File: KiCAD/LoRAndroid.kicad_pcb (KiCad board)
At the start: 4 copper layers, 35 x 14 mm, 55 parts, among them J1 SMA, P1 DX07P022AA6R2000, U1 MIC5504-3.3YMT, U2 SX1262, U3 MCP2210-I-MQ, U4 BGS12SN6, Y1 XRCGB32M000FBH50R0, Y2 CSTCE12M0G15L

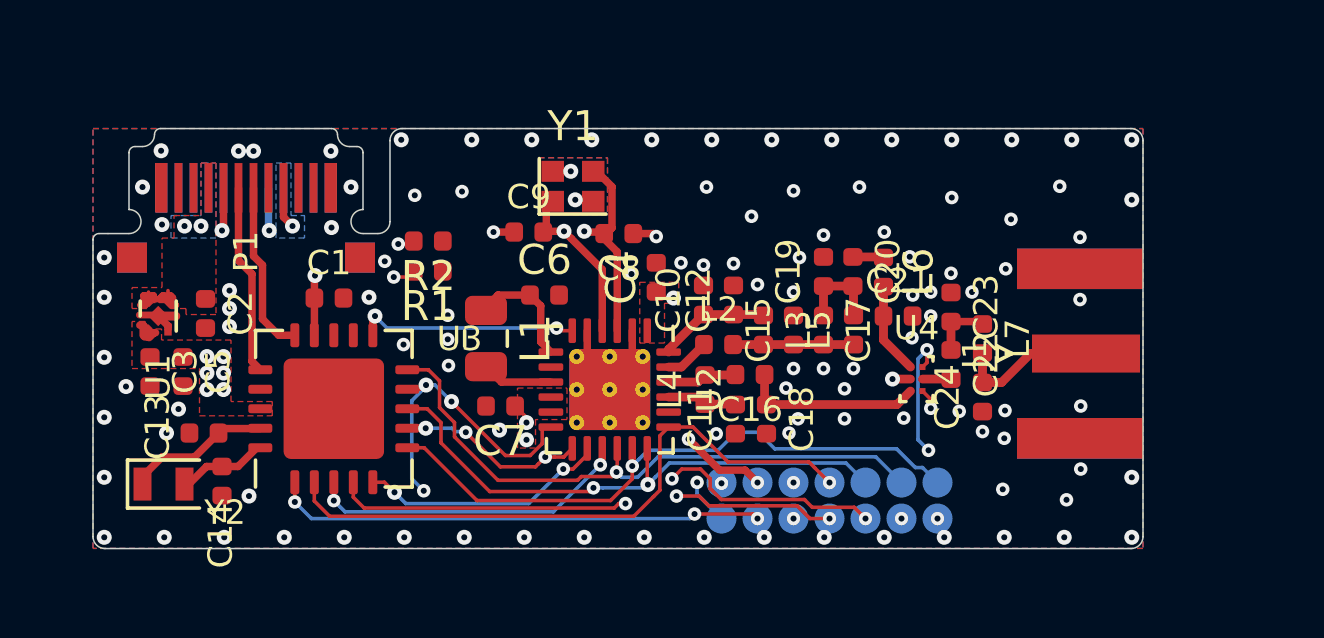
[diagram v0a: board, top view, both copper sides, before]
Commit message: Review, add TVS and mounting holes
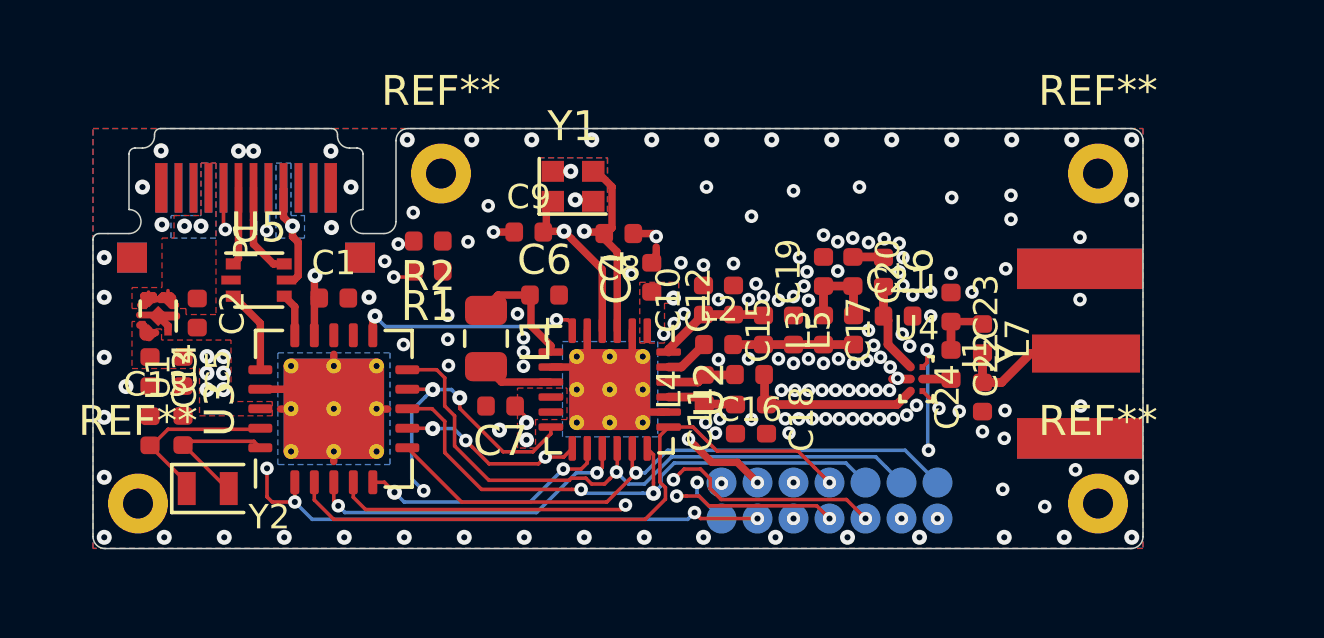
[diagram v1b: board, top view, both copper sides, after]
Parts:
- added REF**: MountingHole_2.2mm_M2_ISO7380, MountingHole:MountingHole_2.2mm_M2_ISO7380, F.Cu at (11.6, 1.50)
- added REF**: MountingHole_2.2mm_M2_ISO7380, MountingHole:MountingHole_2.2mm_M2_ISO7380, F.Cu at (33.5, 1.50)
- added REF**: MountingHole_2.2mm_M2_ISO7380, MountingHole:MountingHole_2.2mm_M2_ISO7380, F.Cu at (33.5, 12.5)
- added REF**: MountingHole_2.2mm_M2_ISO7380, MountingHole:MountingHole_2.2mm_M2_ISO7380, F.Cu at (1.50, 12.5)
- added U5: USBLC6-2P6, Package_TO_SOT_SMD:SOT-666, F.Cu at (5.53, 5.05)
- C15, C18, C23, C24: value - -> DNP
- P1: value DX07P022AA6R2000 -> DX07P022AA6; footprint Connector_USB:USB_C_Plug_JAE_DX07P022AA6R2000 -> Connector_USB:USB_C_Plug_JAE_DX07P022AA6
- TP1, TP10, TP11, TP12, TP15, TP16, TP2, TP3, TP4, TP5, TP6, TP7, TP8, TP9: footprint TestPoint:TestPoint_Pad_D1.0mm -> TestPoint:TestPoint_Pad_D1.0mm_NoCourtyard
- U3: footprint Package_DFN_QFN:QFN-20-1EP_5x5mm_P0.65mm_EP3.35x3.35mm -> Package_DFN_QFN:QFN-20-1EP_5x5mm_P0.65mm_EP3.35x3.35mm_ThermalVias
- moved C14 2.13 mm to (3.00, 10.1), turned to 270 degrees
- moved C13 1.80 mm to (1.90, 10.1), turned to 270 degrees
- moved Y2 1.48 mm to (3.83, 12.0)
- moved P1 0.42 mm to (5.10, 1.98)
- moved C2 0.28 mm to (3.48, 6.15)
- moved C1 0.16 mm to (8.03, 5.65)
- moved C4 0.15 mm to (18.6, 4.96)
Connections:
- P1 pad A6: /D+ -> Net-(P1-PadA6)
- P1 pad A7: /D- -> Net-(P1-PadA7)
- TP16 pad 1: /SPI_~RST -> +3V3
- U3 pad 1: /SPI_~RST -> +3V3
- U3 pad 21: (no net) -> GND
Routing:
- net +3V3: track 26.7 -> 45.2 mm, vias 13 -> 17
- net /SPI_~RST: track 16.4 -> 0.00 mm, vias 3 -> 0
- net /D-: track 5.80 -> 1.45 mm
- net GND: track 8.46 -> 12.2 mm, vias 110 -> 152
- net /D+: track 6.37 -> 2.83 mm
- net Net-(P1-PadA7): track 0.00 -> 3.17 mm
- net Net-(P1-PadA6): track 0.00 -> 2.61 mm
- net /V_USB: track 36.8 -> 38.9 mm
- net Net-(C14-Pad2): track 3.03 -> 4.85 mm
- net /DIO3: track 27.3 -> 29.1 mm
- net Net-(C13-Pad2): track 5.01 -> 5.91 mm
- net /SCK: track 18.7 -> 19.5 mm
- net /MISO: track 20.4 -> 21.1 mm
- net /BUSY: track 18.3 -> 18.9 mm
- net (no net): vias 0 -> 2
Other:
- outline, holes or cut-outs redrawn

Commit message: Update SMA, add POR resistor for MCP2210, small fixes
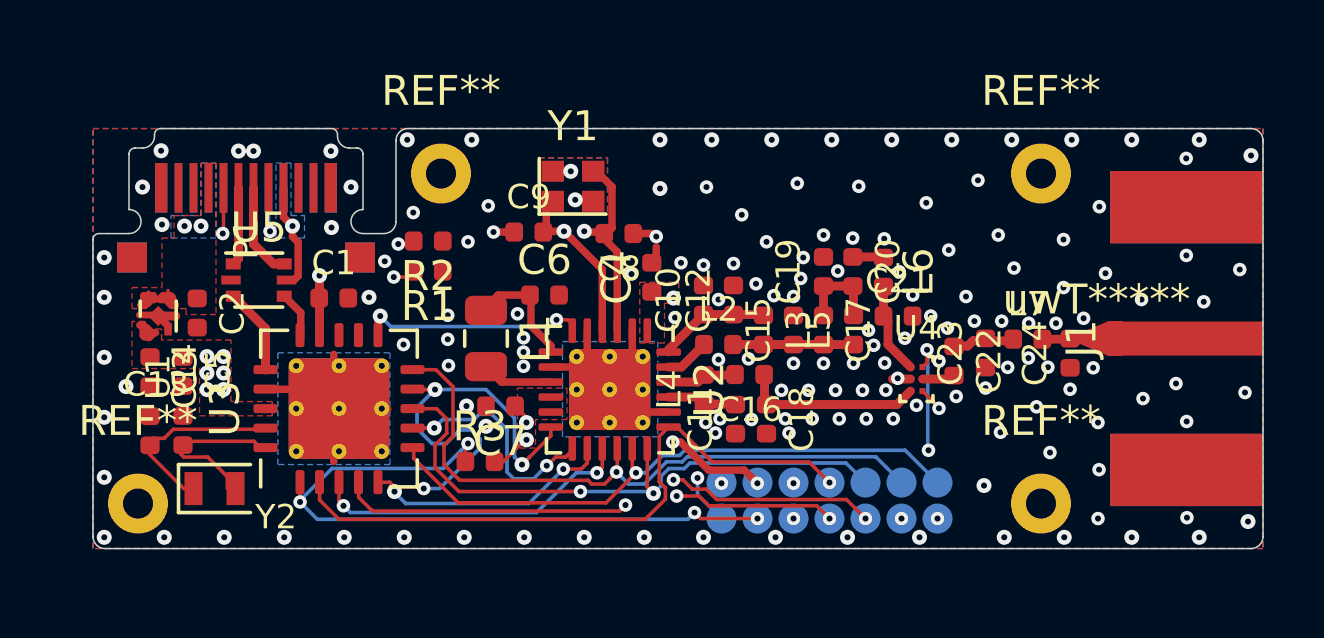
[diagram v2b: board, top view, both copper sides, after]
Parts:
- removed the REF** at (33.5, 1.50)
- removed the REF** at (33.5, 12.5)
- added R3: 1-10k, Resistor_SMD:R_0402_1005Metric, F.Cu at (12.9, 11.1)
- added REF**: MountingHole_2.2mm_M2_ISO7380, MountingHole:MountingHole_2.2mm_M2_ISO7380, F.Cu at (31.6, 12.5)
- added REF**: MountingHole_2.2mm_M2_ISO7380, MountingHole:MountingHole_2.2mm_M2_ISO7380, F.Cu at (31.6, 1.50)
- added uwT*****: uwT0.00_0.30_0.50_1.14_1.25, RF:uwT0.00_0.30_0.50_1.14_1.25, F.Cu at (32.8, 7.00)
- J1: footprint Connector_Coaxial:SMA_Samtec_SMA-J-P-H-ST-EM1_EdgeMount -> Connector_Coaxial:SMA_Cinch_142-0701-881_EdgeMount
- moved J1 3.59 mm to (36.5, 7.00)
- moved C24 3.26 mm to (32.6, 7.49)
- moved C23 1.91 mm to (29.8, 7.48), turned to 90 degrees
- moved L7 1.51 mm to (31.2, 7.02), turned to 0 degrees
- moved Y2 0.22 mm to (4.05, 12.0)
- moved U3 0.17 mm to (8.20, 9.34)
- moved C22 0.15 mm to (28.7, 7.75)
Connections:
- TP16 pad 1: +3V3 -> /SPI_~RST
- U3 pad 1: +3V3 -> /SPI_~RST
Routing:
- net /SPI_~RST: track 0.00 -> 23.3 mm, vias 0 -> 4
- net +3V3: track 45.2 -> 28.9 mm, vias 17 -> 13
- net /DIO2: track 27.1 -> 31.2 mm
- net /DIO1: track 18.5 -> 19.7 mm, vias 5 -> 4
- net /SCK: track 19.5 -> 20.4 mm
- net /MISO: track 21.1 -> 21.9 mm
- net GND: track 12.2 -> 12.1 mm, vias 152 -> 153
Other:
- board size 35 x 14 mm -> 39 x 14 mm
